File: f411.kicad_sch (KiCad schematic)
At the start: 16 parts, among them J18 a8 MCO, J21 Conn_2x02_Pin, SW1 RST, SW2 BT0, U5 STM32F411CEU6

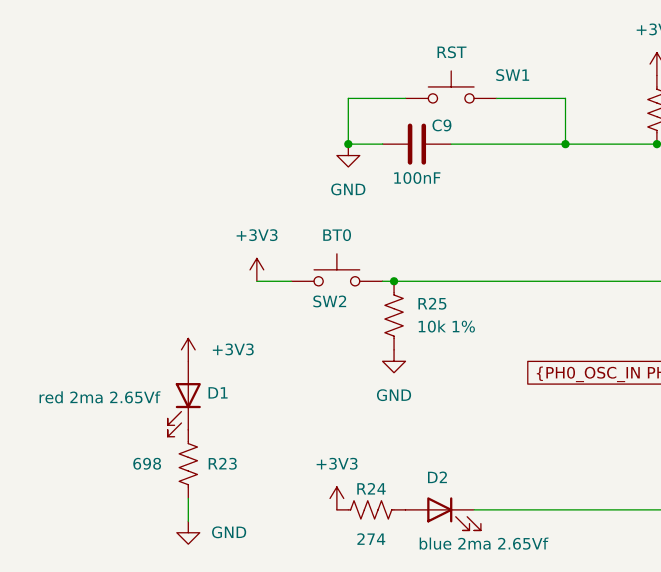
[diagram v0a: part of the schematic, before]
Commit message: BOM cleaned up.
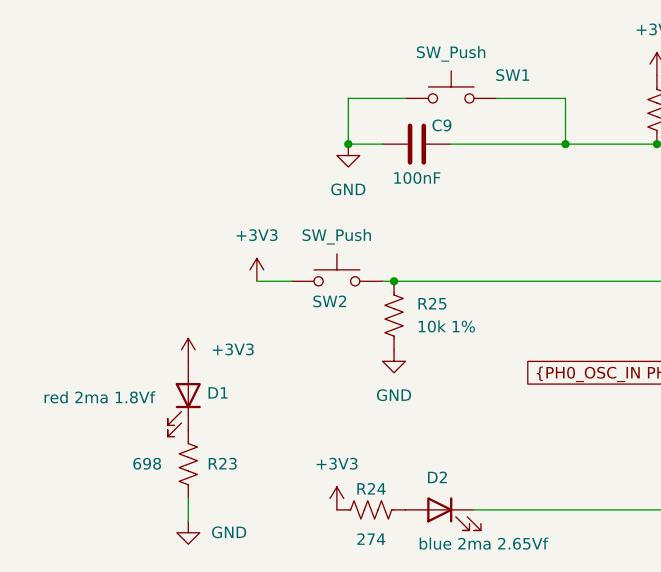
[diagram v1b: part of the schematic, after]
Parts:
- C14, C17, C9: Notes (none) -> or equivalent; Package (none) -> C_0603_1608Metric
- D1: value red 2ma 2.65Vf -> red 2ma 1.8Vf; Package (none) -> LED_0603_1608Metric
- D2: Package (none) -> LED_0603_1608Metric
- J21: Package (none) -> PinSocket_2x02_P2.54mm_Vertical
- L1: Package (none) -> L_0603_1608Metric
- R23, R24, R25, R26, R27: Notes (none) -> or equivalent; Package (none) -> R_0603_1608Metric
- SW1: value RST -> SW_Push; Notes (none) -> or equivalent; Package (none) -> SW_SPST_B3U-1000P
- SW2: value BT0 -> SW_Push; Notes (none) -> or equivalent; Package (none) -> SW_SPST_B3U-1000P
- U5: Package (none) -> QFN-48-1EP_7x7mm_P0.5mm_EP5.6x5.6mm

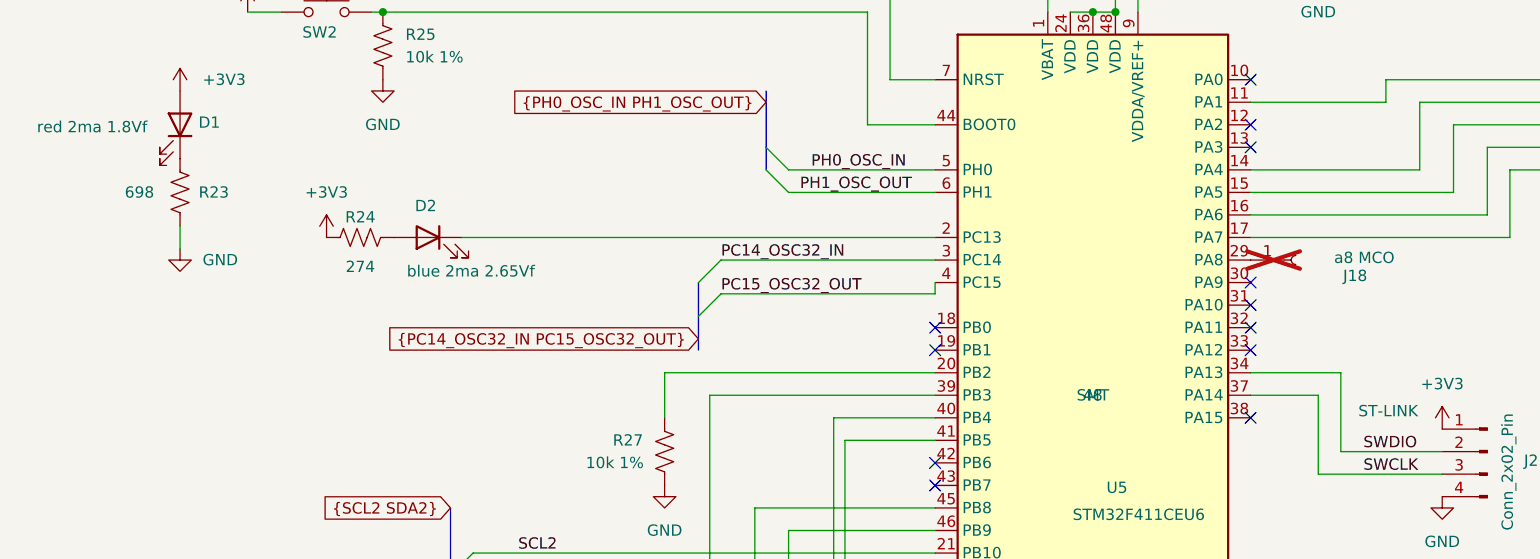
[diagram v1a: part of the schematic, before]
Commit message: added test pad access to PB2 for boot1, renames J18 to TP2.
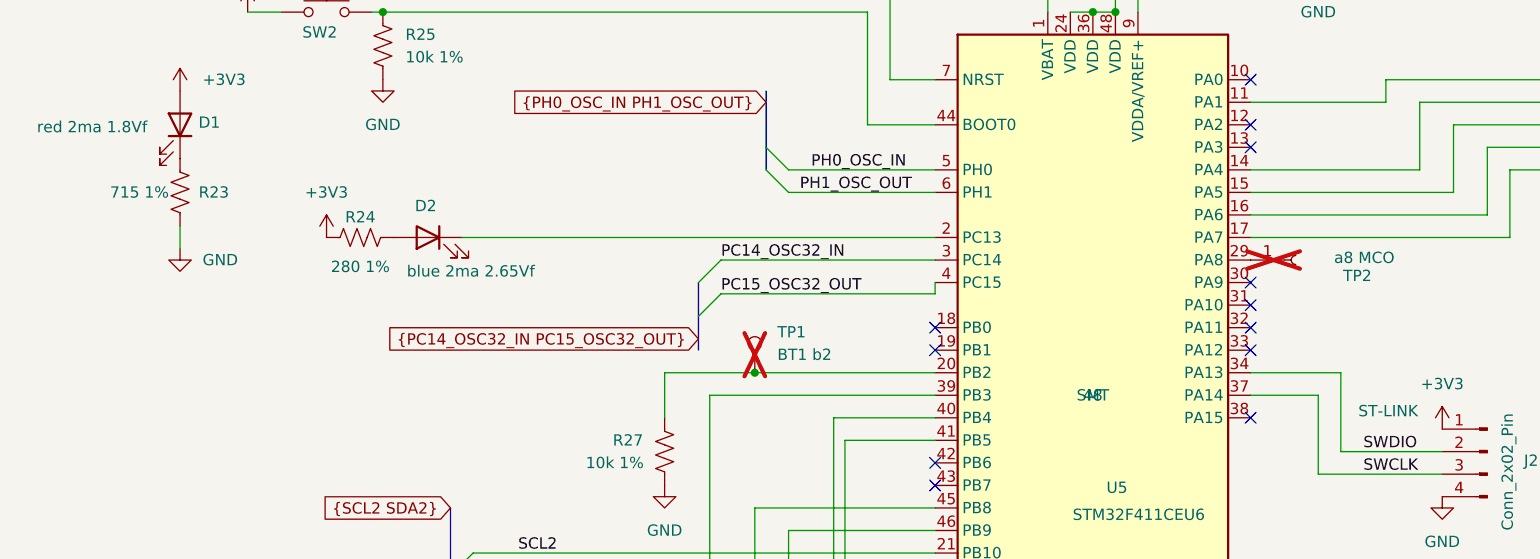
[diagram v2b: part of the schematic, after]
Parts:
- added TP1: BT1 b2, ProjectLib:TestPoint_Pad_D1.0mm, symbol ProjectLib:TestPoint
- D1: MfgPart APTD1608LSECK/J3-PF -> APT1608LSECK/J3-PRV
- D2: MfgPart APHD1608LVBC/D -> APT1608LVBC/D; Notes or equivalent -> or equivalent
- R23: value 698 -> 715 1%; Manufacturer Panasonic -> (none); MfgPart ERJ3EKF6980V -> (none)
- R24: value 274 -> 280 1%; Manufacturer Yageo -> (none); MfgPart RC0603FR-07274RL -> (none)
- TP2: renamed from J18; footprint ProjectLib:TestPoint_THTPad_D1.0mm_Drill0.5mm -> ProjectLib:TestPoint_Pad_D1.0mm
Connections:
- net at R27.1, U5.20 (PB2): now also TP1.1
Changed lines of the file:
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@@
 	)
 	(junction
+		(at 106.68 100.33)
+		(diameter 0)
+		(color 0 0 0 0)
+	)
+	(junction
 		(at 144.78 59.69)
 		(diameter 0)
@@
 	(wire
 		(pts
-			(xy 127 100.33) (xy 96.52 100.33)
-		)
-		(stroke
-			(width 0)
-			(type default)
-		)
-	)
-	(wire
-		(pts
 			(xy 162.56 85.09) (xy 191.77 85.09)
 		)
@@
 	(wire
 		(pts
+			(xy 106.68 100.33) (xy 96.52 100.33)
+		)
+		(stroke
+			(width 0)
+			(type default)
+		)
+	)
+	(wire
+		(pts
 			(xy 162.56 77.47) (xy 181.61 77.47)
 		)
@@
 		)
 	)
+	(wire
+		(pts
+			(xy 106.68 100.33) (xy 127 100.33)
+		)
+		(stroke
+			(width 0)
+			(type default)
+		)
+	)
 	(bus
 		(pts
@@
 		(on_board yes)
 		(dnp yes)
-		(property "Reference" "J18"
+		(property "Reference" "TP2"
 			(at 172.974 89.408 0)
 			(effects
@@
 			)
 		)
-		(property "Footprint" "ProjectLib:TestPoint_THTPad_D1.0mm_Drill0.5mm"
+		(property "Footprint" "ProjectLib:TestPoint_Pad_D1.0mm"
 			(at 167.64 87.63 0)
 			(effects
@@
 			(project "SensorProject_t16-pcb"
 				(path "/0c2d0c14-8850-4a30-bb78-b2f40cb442ba/f12d0b95-be3f-41e2-8b41-943aec5e1edf"
-					(reference "J18")
+					(reference "TP2")
 					(unit 1)
 				)
@@
 			)
 		)
-		(property "MfgPart" "APHD1608LVBC/D"
+		(property "MfgPart" "APT1608LVBC/D"
 			(at 69.85 85.09 0)
 			(effects
@@
 			)
 		)
-		(property "Notes" "or equivalent"
+		(property "Notes" "or equivalent "
 			(at 69.85 85.09 0)
 			(effects
@@
 	)
 	(symbol
+		(lib_id "ProjectLib:TestPoint")
+		(at 106.68 100.33 0)
+		(unit 1)
+		(exclude_from_sim no)
+		(in_bom yes)
+		(on_board yes)
+		(dnp yes)
+		(fields_autoplaced yes)
+		(property "Reference" "TP1"
+			(at 109.22 95.7579 0)
+			(effects
+				(font
+					(size 1.27 1.27)
+				)
+				(justify left)
+			)
+		)
+		(property "Value" "BT1  b2"
+			(at 109.22 98.2979 0)
+			(effects
+				(font
+					(size 1.27 1.27)
+				)
+				(justify left)
+			)
+		)
+		(property "Footprint" "ProjectLib:TestPoint_Pad_D1.0mm"
+			(at 111.76 100.33 0)
+			(effects
+				(font
+					(size 1.27 1.27)
+				)
+				(hide yes)
+			)
+		)
+		(property "Datasheet" "~"
+			(at 111.76 100.33 0)
+			(effects
+				(font
+					(size 1.27 1.27)
+				)
+				(hide yes)
+			)
+		)
+		(property "Description" "test point"
+			(at 106.68 100.33 0)
+			(effects
+				(font
+					(size 1.27 1.27)
+				)
+				(hide yes)
+			)
+		)
+		(pin "1"
+		)
+		(instances
+			(project ""
+				(path "/0c2d0c14-8850-4a30-bb78-b2f40cb442ba/f12d0b95-be3f-41e2-8b41-943aec5e1edf"
+					(reference "TP1")
+					(unit 1)
+				)
+			)
+		)
+	)
+	(symbol
 		(lib_id "power:GND")
 		(at 139.7 143.51 0)
@@
 			)
 		)
-		(property "MfgPart" "APTD1608LSECK/J3-PF"
+		(property "MfgPart" "APT1608LSECK/J3-PRV"
 			(at 41.91 72.39 0)
 			(effects
@@
 			)
 		)
-		(property "Value" "274"
+		(property "Value" "280 1%"
 			(at 62.23 88.392 90)
 			(effects
@@
 			)
 		)
-		(property "Manufacturer" "Yageo"
+		(property "Manufacturer" ""
 			(at 62.23 85.09 90)
 			(effects
@@
 			)
 		)
-		(property "MfgPart" "RC0603FR-07274RL"
+		(property "MfgPart" ""
 			(at 62.23 85.09 90)
 			(effects
@@
 			)
 		)
-		(property "Value" "698"
+		(property "Value" "715 1%"
 			(at 37.338 80.01 0)
 			(effects
@@
 			)
 		)
-		(property "Manufacturer" "Panasonic"
+		(property "Manufacturer" ""
 			(at 41.91 80.01 0)
 			(effects
@@
 			)
 		)
-		(property "MfgPart" "ERJ3EKF6980V"
+		(property "MfgPart" ""
 			(at 41.91 80.01 0)
 			(effects

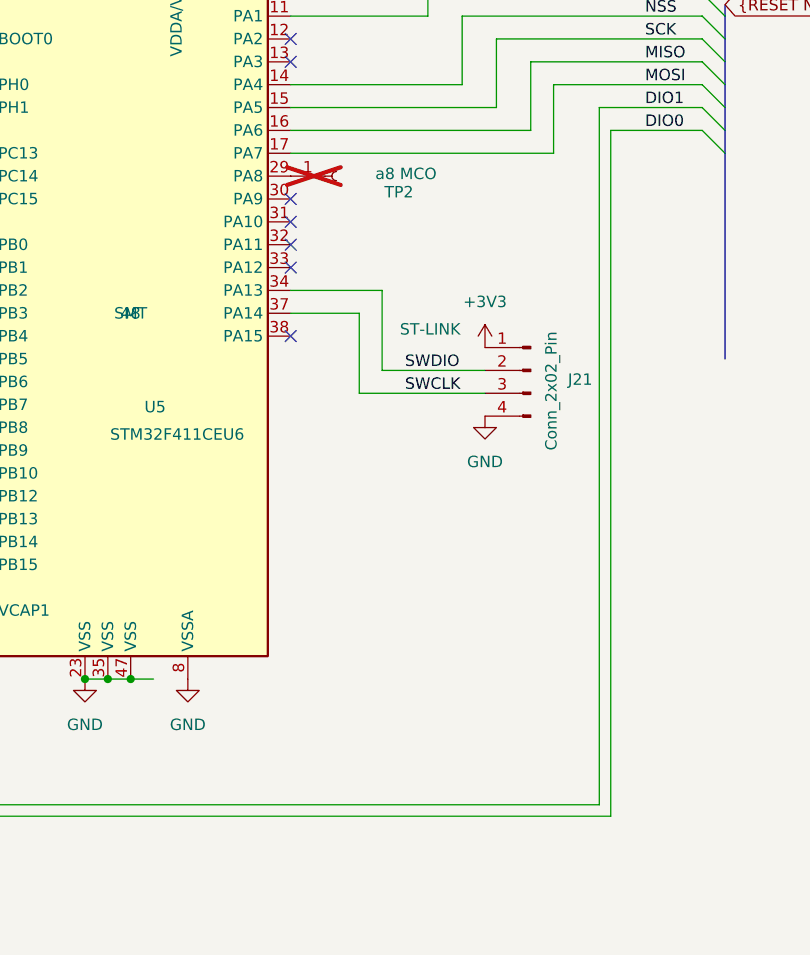
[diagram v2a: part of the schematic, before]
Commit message: flip side for radio in progress.
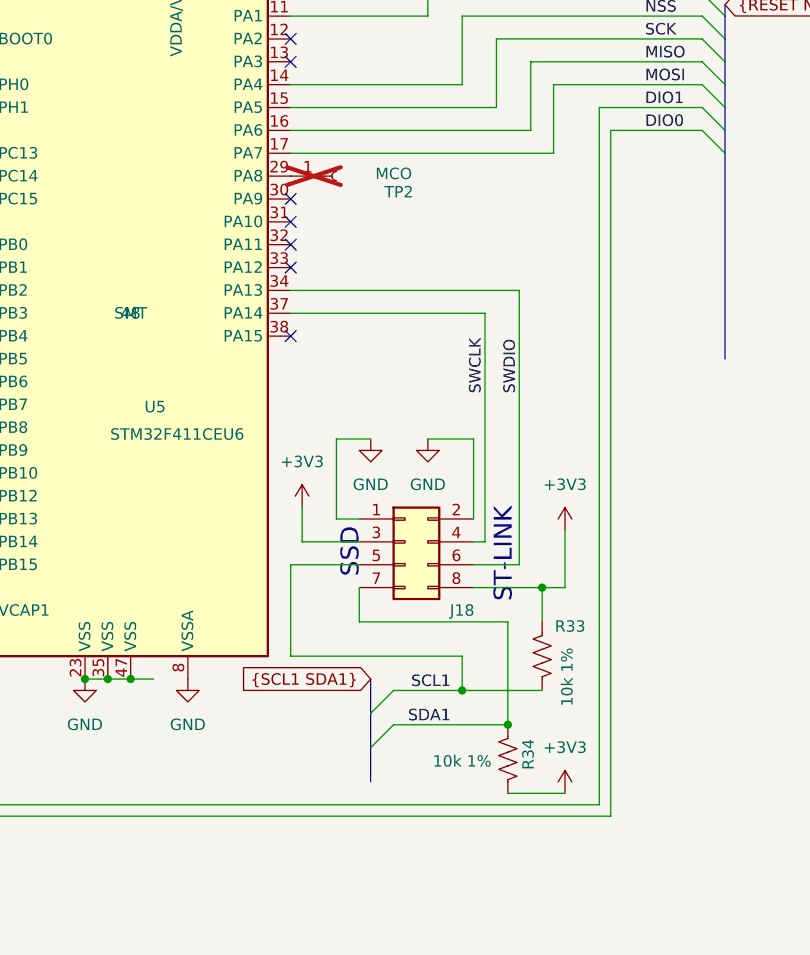
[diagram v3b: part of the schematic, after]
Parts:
- removed J21: Conn_2x02_Pin, ProjectLib:PinSocket_2x02_P2.54mm_Vertical, symbol ProjectLib:Conn_01x04_Pin
- added J18: Conn_02x04_Top_Bottom, ProjectLib:PinHeader_2x04_P2.54mm_Vertical_SMD, symbol ProjectLib:Conn_02x04_Odd_Even
- added R33, R34: 10k 1%, ProjectLib:R_0603_1608Metric, symbol ProjectLib:R_US
- TP2: value a8 MCO -> MCO
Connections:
- net +3V3: now also J18.3 (Pin_3), J18.8 (Pin_8), R33.1, R34.2
- net GND: now also J18.1 (Pin_1), J18.2 (Pin_2)
- net SCL1: now also J18.5 (Pin_5), R33.2
- net SDA1: now also J18.7 (Pin_7), R34.1
- net SWCLK: now also J18.4 (Pin_4)
- net SWDIO: now also J18.6 (Pin_6)
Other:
- note added: "SSD"
- note added: "ST-LINK"

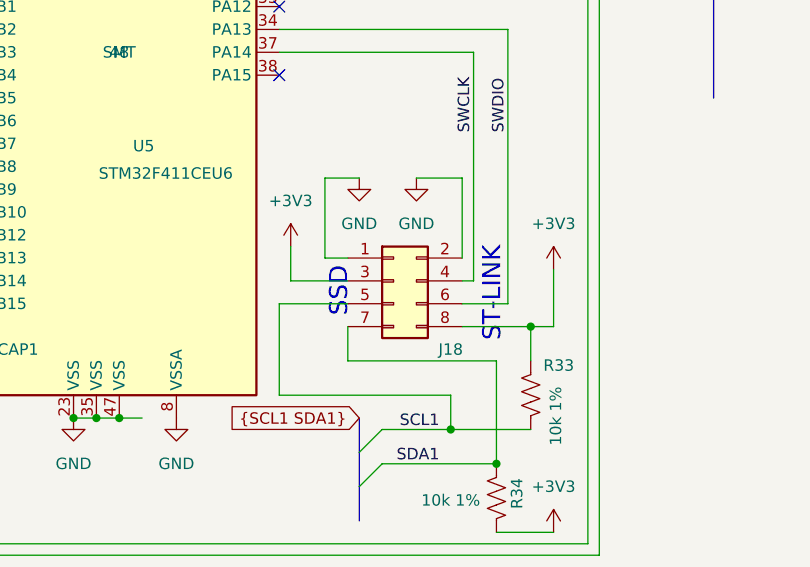
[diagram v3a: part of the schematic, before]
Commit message: finished flipping radio side.
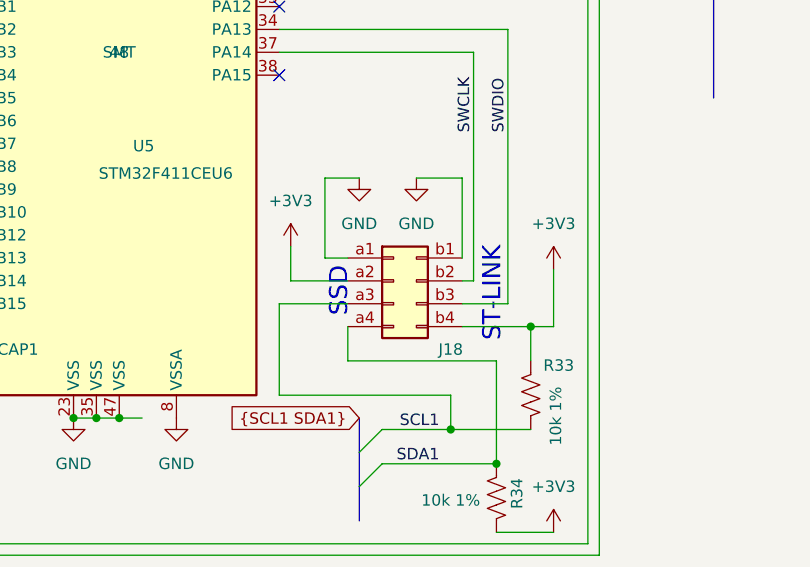
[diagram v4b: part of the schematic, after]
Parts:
- J18: footprint ProjectLib:PinHeader_2x04_P2.54mm_Vertical_SMD -> ProjectLib:PinSocket_2x04_P2.54mm_Vertical_SMD; symbol ProjectLib:Conn_02x04_Odd_Even -> ProjectLib:Conn_02x04_Row_Letter_First
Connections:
- net +3V3: now also J18.a2 (Pin_a2), J18.b4 (Pin_b4); no longer J18.3 (Pin_3), J18.8 (Pin_8)
- net GND: now also J18.a1 (Pin_a1), J18.b1 (Pin_b1); no longer J18.1 (Pin_1), J18.2 (Pin_2)
- net SCL1: now also J18.a3 (Pin_a3); no longer J18.5 (Pin_5)
- net SDA1: now also J18.a4 (Pin_a4); no longer J18.7 (Pin_7)
- net SWCLK: now also J18.b2 (Pin_b2); no longer J18.4 (Pin_4)
- net SWDIO: now also J18.b3 (Pin_b3); no longer J18.6 (Pin_6)
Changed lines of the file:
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@@
 	)
 	(symbol
-		(lib_id "ProjectLib:Conn_02x04_Odd_Even")
+		(lib_id "ProjectLib:Conn_02x04_Row_Letter_First")
 		(at 175.26 128.27 0)
 		(unit 1)
@@
 			)
 		)
-		(property "Footprint" "ProjectLib:PinHeader_2x04_P2.54mm_Vertical_SMD"
+		(property "Footprint" "ProjectLib:PinSocket_2x04_P2.54mm_Vertical_SMD"
 			(at 175.26 128.27 0)
 			(effects
@@
 			)
 		)
-		(property "Description" "Generic connector, double row, 02x04, odd/even pin numbering scheme (row 1 odd numbers, row 2 even numbers), script generated (kicad-library-utils/schlib/autogen/connector/)"
+		(property "Description" "Generic connector, double row, 02x04, row letter first pin numbering scheme (pin number consists of a letter for the row and a number for the pin index in this row. a1, ..., aN; b1, ..., bN), script generated (kicad-library-utils/schlib/autogen/connector/)"
 			(at 175.26 128.27 0)
 			(effects
@@
 			)
 		)
-		(pin "4"
+		(pin "a1"
 		)
-		(pin "2"
+		(pin "b4"
 		)
-		(pin "1"
+		(pin "a4"
 		)
-		(pin "3"
+		(pin "b3"
 		)
-		(pin "8"
+		(pin "b1"
 		)
-		(pin "5"
+		(pin "b2"
 		)
-		(pin "6"
+		(pin "a2"
 		)
-		(pin "7"
+		(pin "a3"
 		)
 		(instances
